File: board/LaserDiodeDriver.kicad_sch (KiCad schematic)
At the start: 55 parts, among them J1 Conn_01x02, K1 EE2-12NU, Q1 2N7002, Q2 IRF9Z34, SW1 SW_SPDT, U1 LT1009, U2 OPA4192, U3 LM317_TO-220

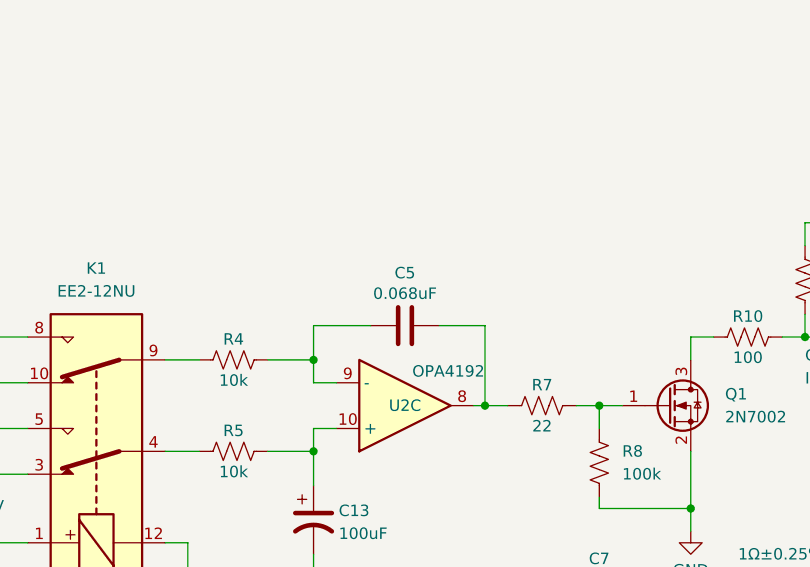
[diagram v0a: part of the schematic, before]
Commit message: Changed gate drive feedback capacitor and tested constant power control. Needs improvement.
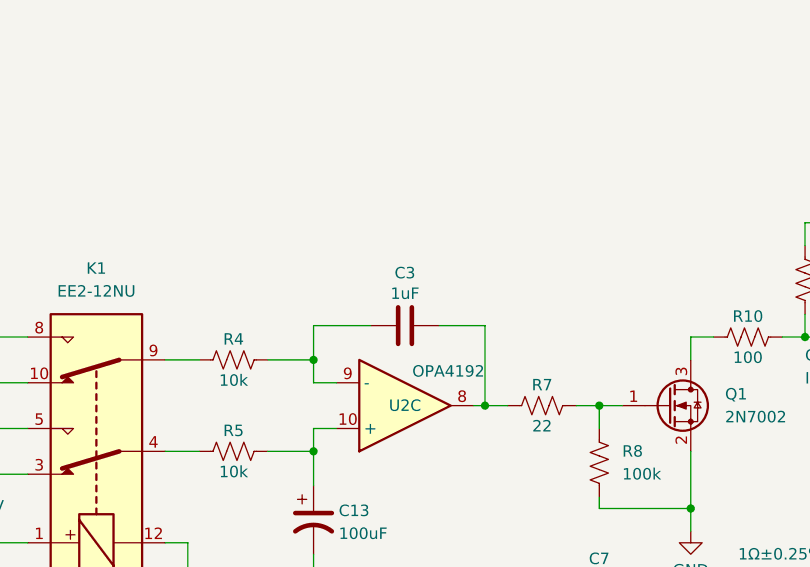
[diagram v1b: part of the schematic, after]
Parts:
- removed C5: 0.068uF, Capacitor_SMD:C_0603_1608Metric, symbol Device:C
- added C3: 1uF, Capacitor_SMD:C_0603_1608Metric, symbol Device:C
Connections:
- net at R4.2, U2.9 (-): now also C3.1
- net at R7.1, U2.8: now also C3.2
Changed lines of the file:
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@@
-	)
-	(symbol
-		(lib_id "Device:C")
-		(at 80.01 106.68 90)
-		(unit 1)
-		(exclude_from_sim no)
-		(in_bom yes)
-		(on_board yes)
-		(dnp no)
-		(property "Reference" "C5"
-			(at 80.01 100.838 90)
-			(effects
-				(font
-					(size 1.27 1.27)
-				)
-			)
-		)
-		(property "Value" "0.068uF"
-			(at 80.01 103.124 90)
-			(effects
-				(font
-					(size 1.27 1.27)
-				)
-			)
-		)
-		(property "Footprint" "Capacitor_SMD:C_0603_1608Metric"
-			(at 83.82 105.7148 0)
-			(effects
-				(font
-					(size 1.27 1.27)
-				)
-				(hide yes)
-			)
-		)
-		(property "Datasheet" "https://www.digikey.com/en/products/detail/w%C3%BCrth-elektronik/885012206094/5453867"
-			(at 80.01 106.68 0)
-			(effects
-				(font
-					(size 1.27 1.27)
-				)
-				(hide yes)
-			)
-		)
-		(property "Description" "0.068 µF ±10% 50V Ceramic Capacitor X7R 0603 (1608 Metric)"
-			(at 80.01 106.68 0)
-			(effects
-				(font
-					(size 1.27 1.27)
-				)
-				(hide yes)
-			)
-		)
-		(property "Price" "$0.10000"
-			(at 80.01 106.68 90)
-			(effects
-				(font
-					(size 1.27 1.27)
-				)
-				(hide yes)
-			)
-		)
-		(pin "1"
-		)
-		(pin "2"
-		)
-		(instances
-			(project "LaserDiodeDriver"
-				(path "/331385f6-e980-45c6-bdf7-9362279e36d1"
-					(reference "C5")
-					(unit 1)
-				)
-			)
-		)
 	)
 	(symbol
@@
 					(unit 1)
 				)
+			)
+		)
+	)
+	(symbol
+		(lib_id "Device:C")
+		(at 80.01 106.68 90)
+		(unit 1)
+		(exclude_from_sim no)
+		(in_bom yes)
+		(on_board yes)
+		(dnp no)
+		(property "Reference" "C3"
+			(at 80.01 100.838 90)
+			(effects
+				(font
+					(size 1.27 1.27)
+				)
+			)
+		)
+		(property "Value" "1uF"
+			(at 80.01 103.124 90)
+			(effects
+				(font
+					(size 1.27 1.27)
+				)
+			)
+		)
+		(property "Footprint" "Capacitor_SMD:C_0603_1608Metric"
+			(at 83.82 105.7148 0)
+			(effects
+				(font
+					(size 1.27 1.27)
+				)
+				(hide yes)
+			)
+		)
+		(property "Datasheet" "(Standards)"
+			(at 80.01 106.68 0)
+			(effects
+				(font
+					(size 1.27 1.27)
+				)
+				(hide yes)
+			)
+		)
+		(property "Description" "1uF, 50V, 0603 (Standards)"
+			(at 80.01 106.68 0)
+			(effects
+				(font
+					(size 1.27 1.27)
+				)
+				(hide yes)
+			)
+		)
+		(pin "1"
+		)
+		(pin "2"
+		)
+		(instances
+			(project "LaserDiodeDriver"
+				(path "/331385f6-e980-45c6-bdf7-9362279e36d1"
+					(reference "C3")
+					(unit 1)
+				)

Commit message: Imported power connector models and info.
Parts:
- J1: footprint Connector_Hirose:Hirose_DF13-02P-1.25DS_1x02_P1.25mm_Horizontal -> Connector_JST:JST_EH_S2B-EH_1x02_P2.50mm_Horizontal; Crimp https://www.digikey.com/en/products/detail/hirose-electric-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 -> https://www.digikey.com/en/products/detail/jst-sales-americ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; Mate https://www.digikey.com/en/products/detail/hirose-electric-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 -> https://www.digikey.com/en/products/detail/jst-sales-americ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; Price $0.46000 -> $0.10000
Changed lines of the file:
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@@
 			)
 		)
-		(property "Footprint" "Connector_Hirose:Hirose_DF13-02P-1.25DS_1x02_P1.25mm_Horizontal"
+		(property "Footprint" "Connector_JST:JST_EH_S2B-EH_1x02_P2.50mm_Horizontal"
 			(at 41.91 43.18 0)
 			(effects
@@
 			)
 		)
-		(property "Datasheet" "https://www.digikey.com/en/products/detail/hirose-electric-co-ltd/DF3-2P-2DS-01/455725"
+		(property "Datasheet" "https://www.digikey.com/en/products/detail/jst-sales-america-inc/S2B-EH/926533"
 			(at 41.91 43.18 0)
 			(effects
@@
 			)
 		)
-		(property "Price" " $0.46000"
+		(property "Price" " $0.10000"
 			(at 41.91 43.18 0)
 			(effects
@@
 			)
 		)
-		(property "Mate" "https://www.digikey.com/en/products/detail/hirose-electric-co-ltd/DF3-2S-2C/141479"
+		(property "Mate" "https://www.digikey.com/en/products/detail/jst-sales-america-inc/EHR-2/527224"
 			(at 41.91 43.18 0)
 			(effects
@@
 			)
 		)
-		(property "Crimp" "https://www.digikey.com/en/products/detail/hirose-electric-co-ltd/DF3-2428SCC/269904"
+		(property "Crimp" "https://www.digikey.com/en/products/detail/jst-sales-america-inc/SEH-001T-P0-6/26213194"
 			(at 41.91 43.18 0)
 			(effects

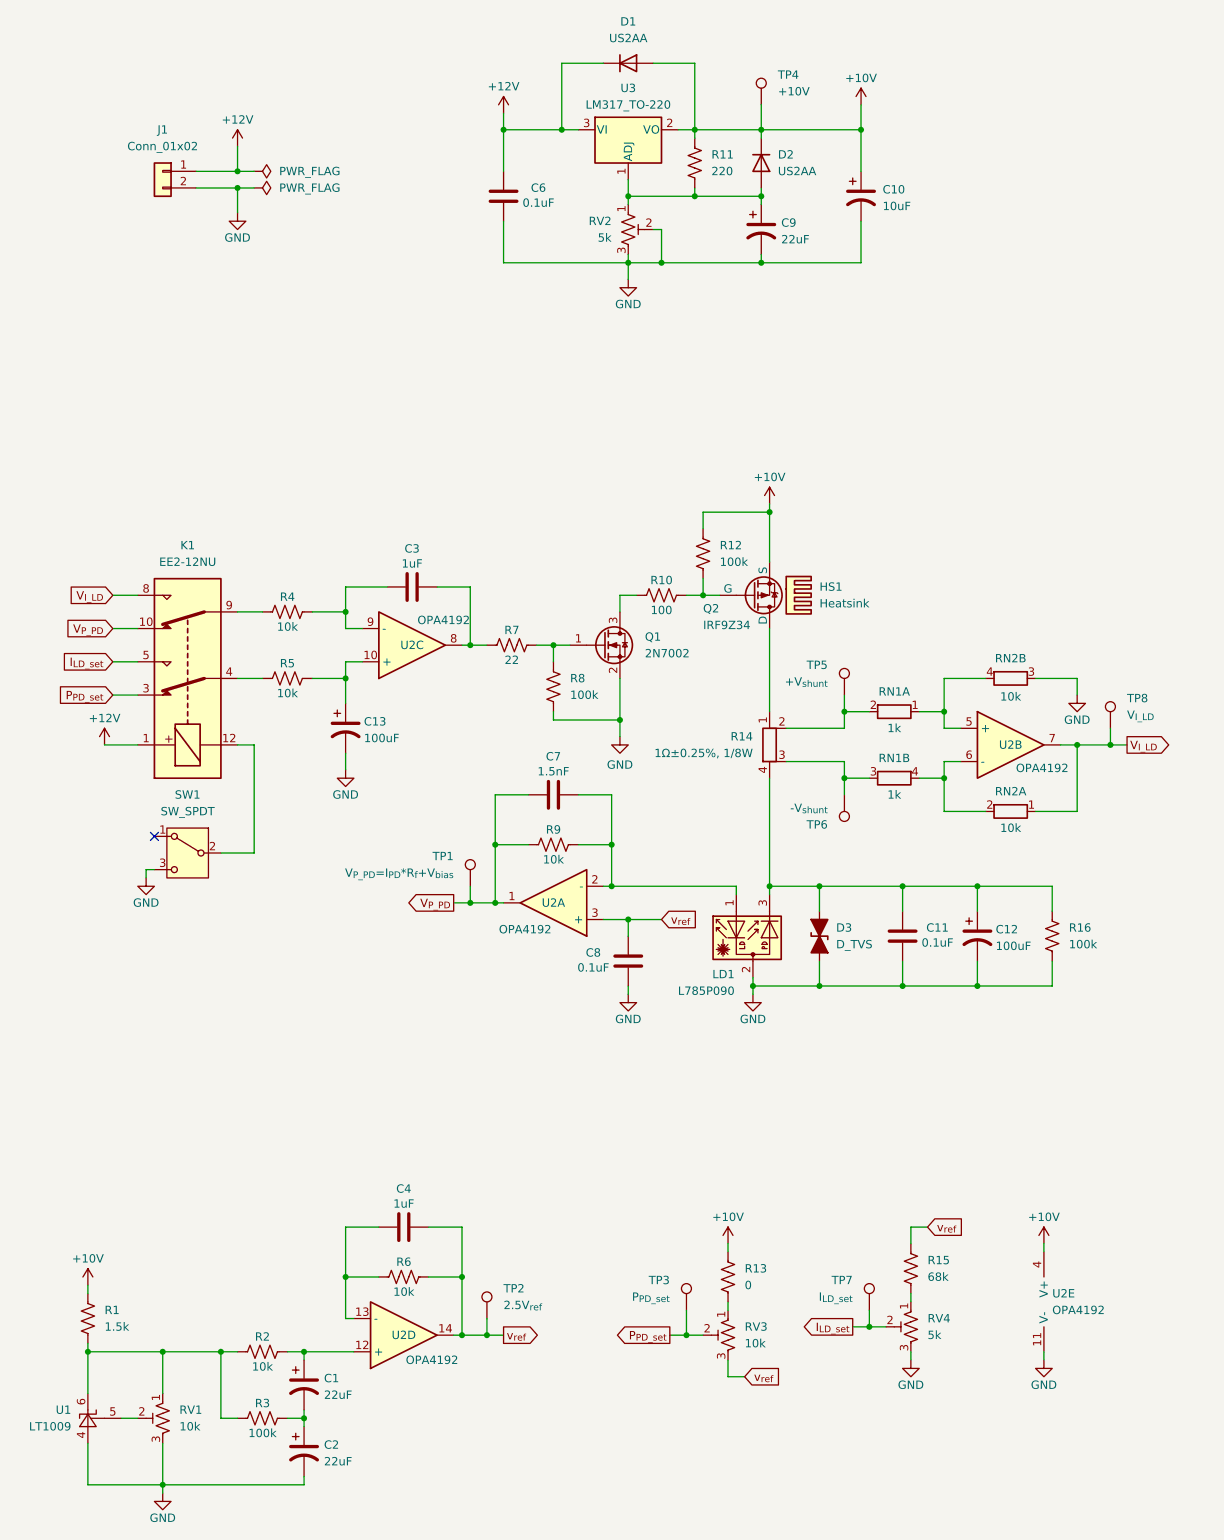
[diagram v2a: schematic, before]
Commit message: Layout of differential amplifier, TIA, and laser diode.
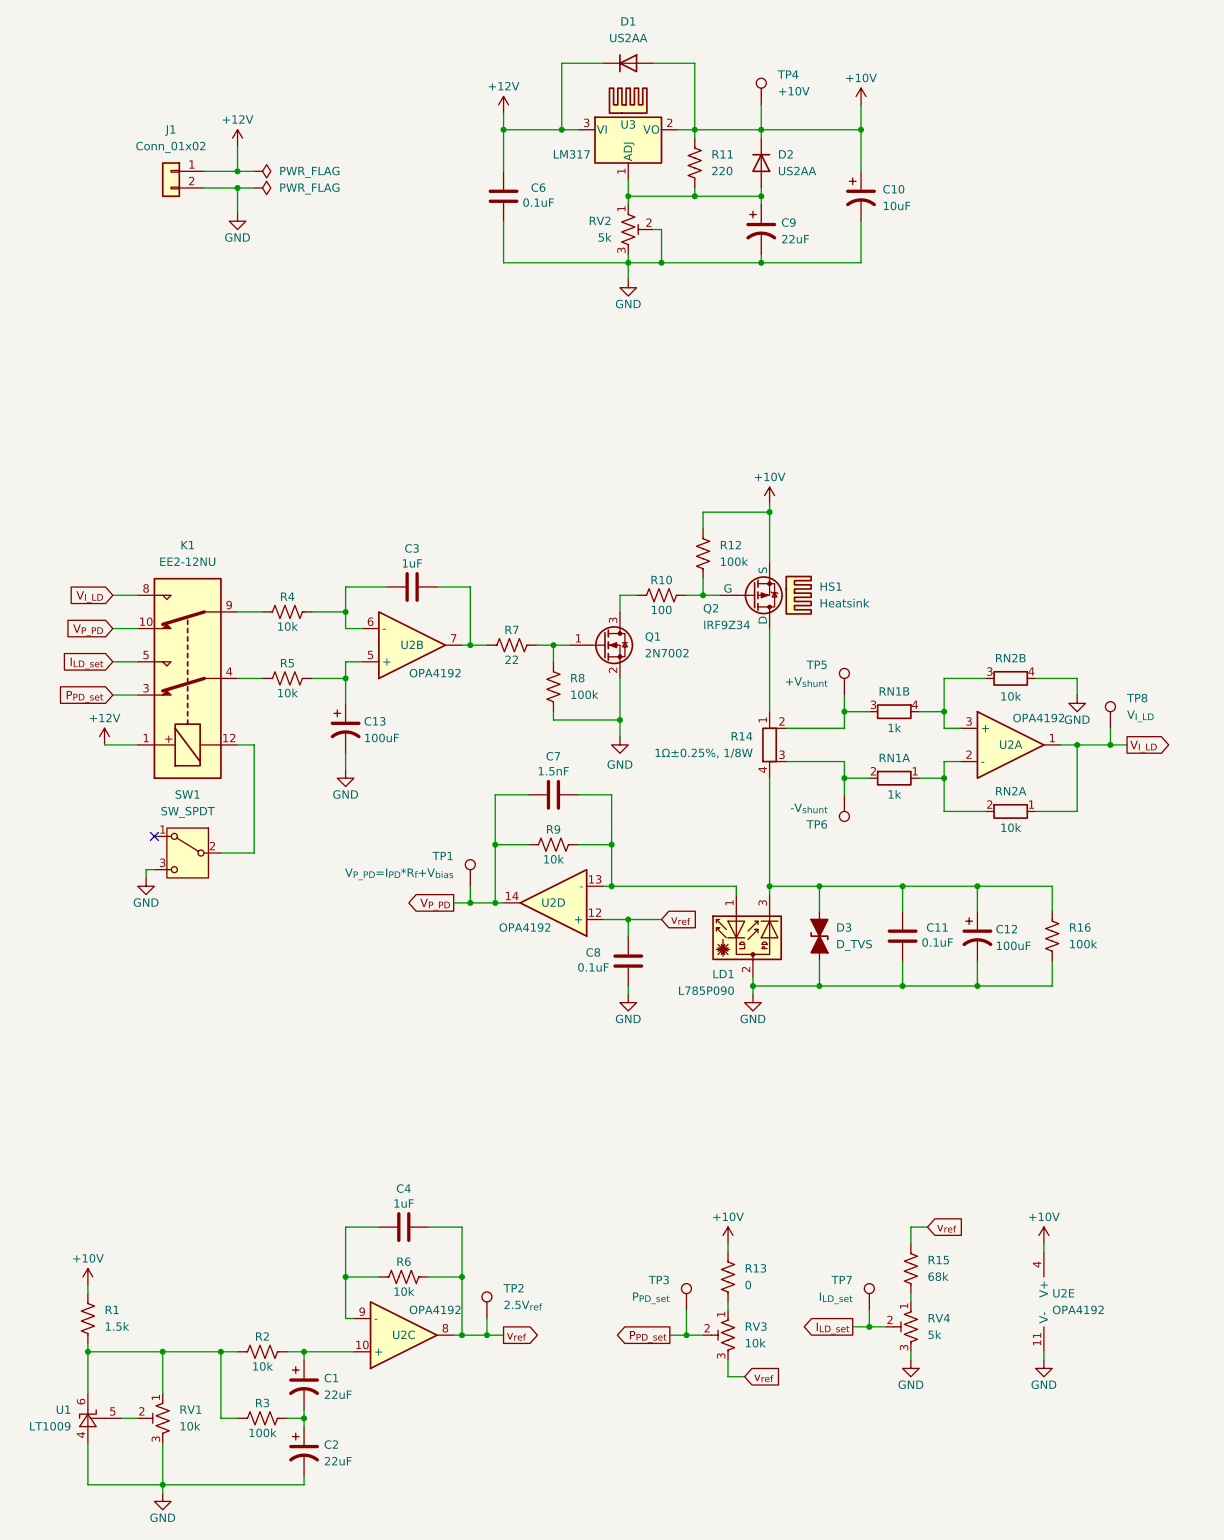
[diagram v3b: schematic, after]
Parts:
- added HS2: Heatsink, symbol Mechanical:Heatsink
- U3: value LM317_TO-220 -> LM317
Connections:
- net GND: now also RN2.4 (R2.2); no longer RN2.3 (R2.1)
- net V_{I_LD}: now also U2.1; no longer U2.7
- net V_{P_PD}: now also U2.14; no longer U2.1
- net v_{ref}: now also U2.12 (+), U2.8; no longer U2.14, U2.3 (+)
- net at C13.1, R5.2: now also U2.5 (+); no longer U2.10 (+)
- net at C3.2, R7.1: now also U2.7; no longer U2.8
- net at C3.1, R4.2: now also U2.6 (-); no longer U2.9 (-)
- net at R14.2, TP5.1: now also RN1.3 (R2.1); no longer RN1.2 (R1.2)
- net at C7.2, LD1.1, R9.2: now also U2.13 (-); no longer U2.2 (-)
- net at C4.1, R6.1: now also U2.9 (-); no longer U2.13 (-)
- net at R14.3, TP6.1: now also RN1.2 (R1.2); no longer RN1.3 (R2.1)
- net at C1.1, R2.2: now also U2.10 (+); no longer U2.12 (+)
- new net: RN1.1 (R1.1), RN2.2 (R1.2), U2.2 (-)
- new net: RN1.4 (R2.2), RN2.3 (R2.1), U2.3 (+)
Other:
- moved on the sheet: J1, RN1A, RN1B, RN2B, U2A, U2B, U2C, U2D

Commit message: Added laser diode 3D file and more layout
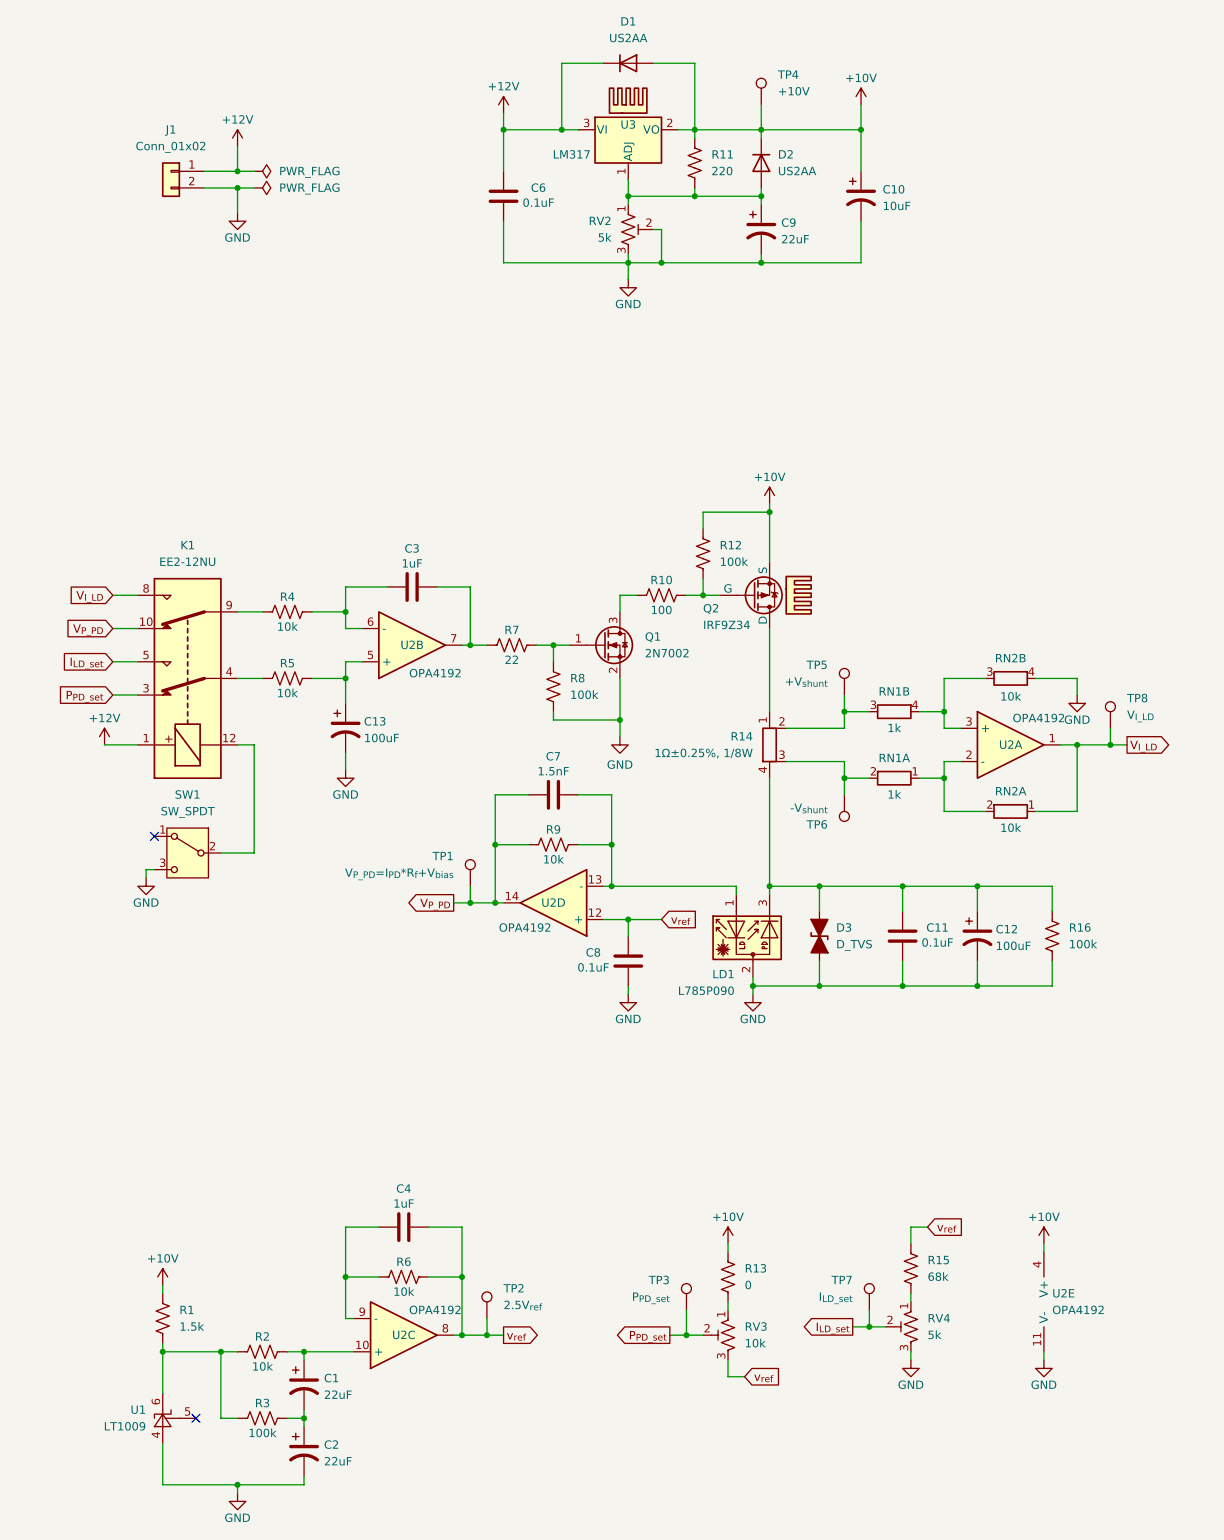
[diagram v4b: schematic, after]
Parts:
- removed RV1: 10k, Potentiometer_THT:Potentiometer_Bourns_3296W_Vertical, symbol Device:R_Potentiometer_Trim_US
- HS1: footprint Heatsink:Heatsink_AAVID_Extruded_531002B00000G_34.9x12.7mm_H25.4mm -> (none); Price $1.72000 -> (none)
- Q2, U3: footprint Package_TO_SOT_THT:TO-220-3_Vertical -> Package_TO_SOT_THT:TO-220-3_Horizontal_TabUp
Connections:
- no-connect marks 1 -> 2
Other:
- moved on the sheet: R1, U1
